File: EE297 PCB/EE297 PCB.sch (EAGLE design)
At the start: 98 parts, among them IC1 MEGA32-P, IC2 MEGA32-P, IC3 7805T, K1 CQ1-12V, K3 CQ1-12V, T1 BC547, T2 TIP122, T3 TIP122, T4 TIP122, T5 BC547

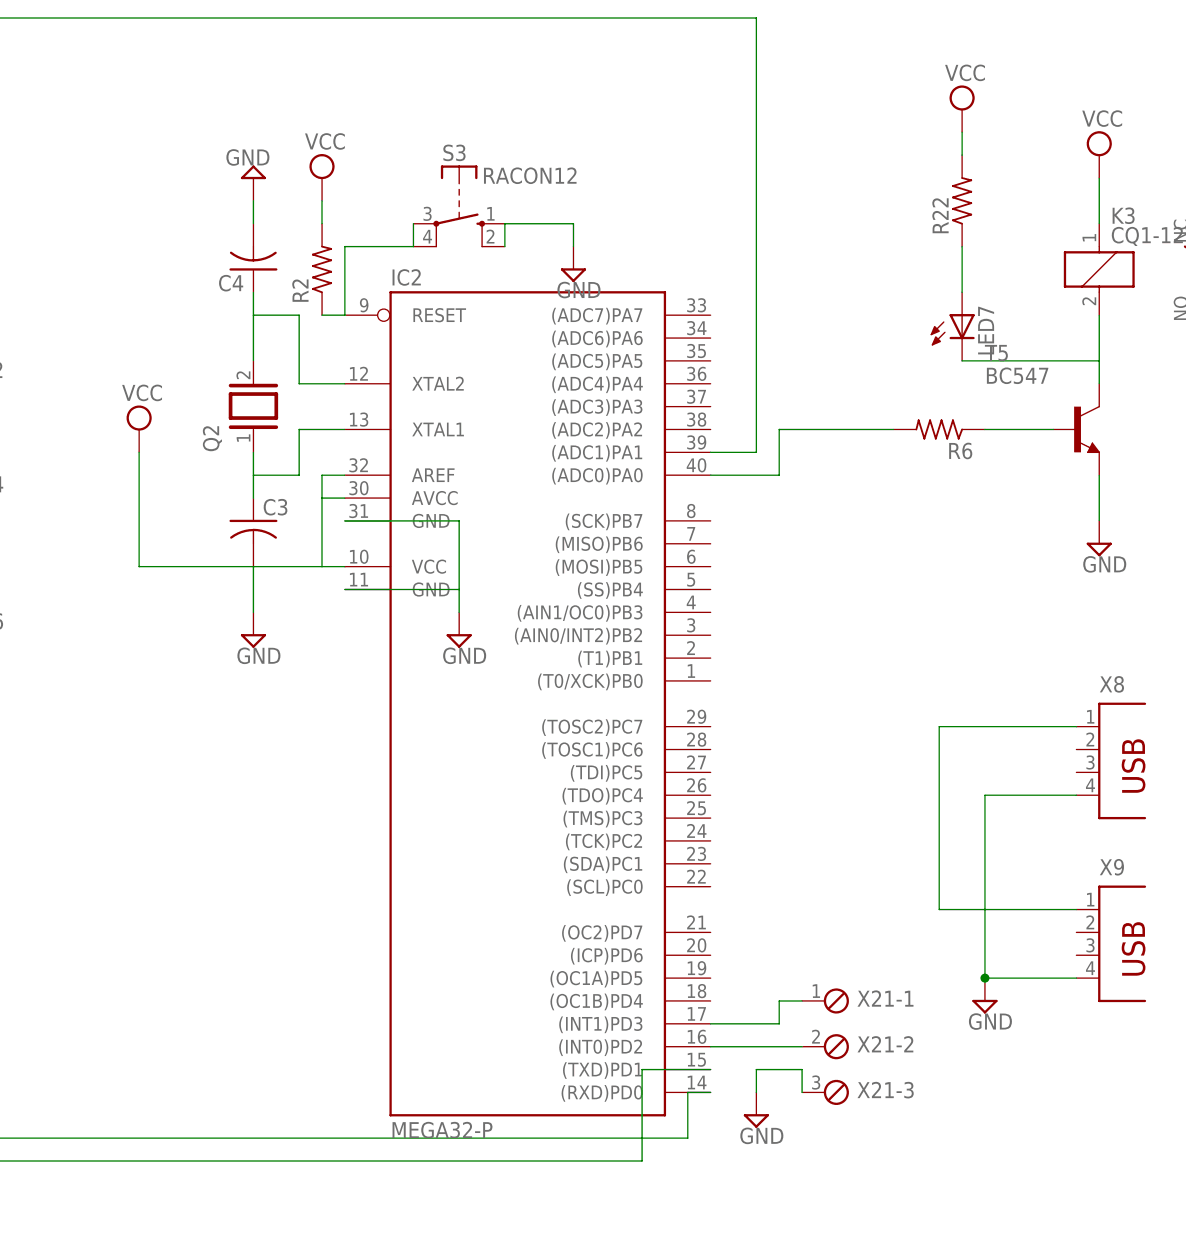
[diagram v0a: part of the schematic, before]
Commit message: MS Project PCB Design Added
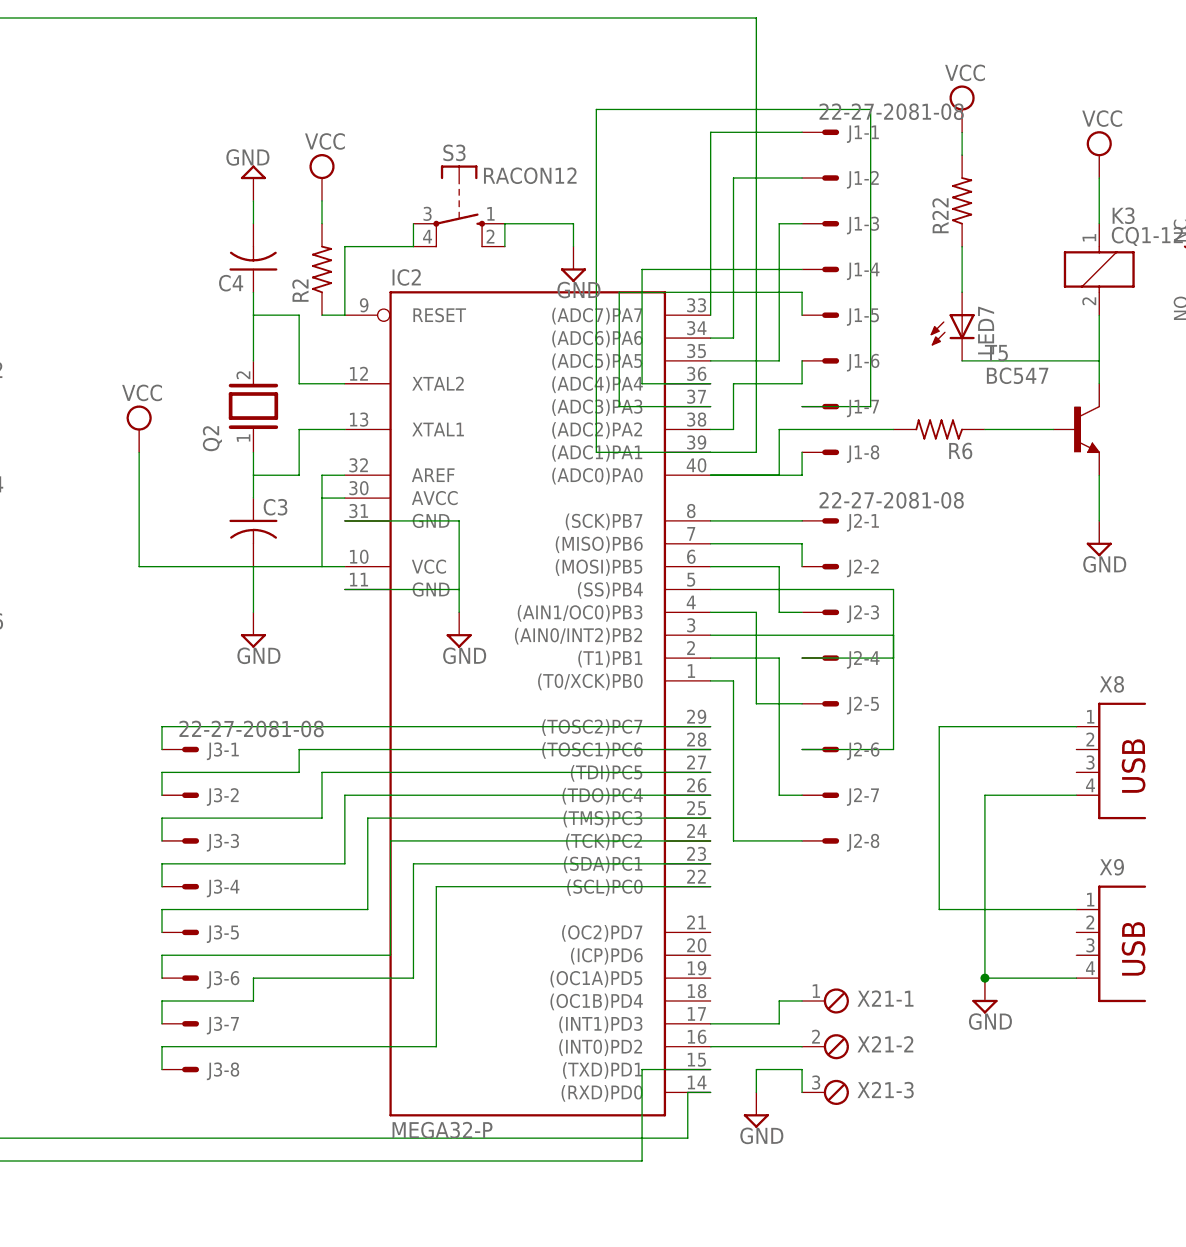
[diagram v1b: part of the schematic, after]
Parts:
- added J1, J2, J3: 22-27-2081-08, con-molex:22-27-2081-08
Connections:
- new net N$157: IC2.(ADC7)PA7, J1-1.S
- new net N$158: IC2.(ADC6)PA6, J1-2.S
- new net N$159: IC2.(ADC5)PA5, J1-3.S
- new net N$160: IC2.(ADC4)PA4, J1-4.S
- new net N$161: IC2.(ADC3)PA3, J1-5.S
- new net N$162: IC2.(ADC2)PA2, J1-6.S
- new net N$164: IC2.(SCK)PB7, J2-1.S
- new net N$165: IC2.(MISO)PB6, J2-2.S
- new net N$166: IC2.(MOSI)PB5, J2-3.S
- new net N$167: IC2.(SS)PB4, J2-4.S
- new net N$168: IC2.(AIN1/OC0)PB3, J2-5.S
- new net N$169: IC2.(AIN0/INT2)PB2, J2-6.S
- new net N$170: IC2.(T1)PB1, J2-7.S
- new net N$171: IC2.(T0/XCK)PB0, J2-8.S
- new net N$172: IC2.(TOSC2)PC7, J3-1.S
- new net N$173: IC2.(TOSC1)PC6, J3-2.S
- new net N$174: IC2.(TDI)PC5, J3-3.S
- new net N$175: IC2.(TDO)PC4, J3-4.S
- new net N$176: IC2.(TMS)PC3, J3-5.S
- new net N$177: IC2.(TCK)PC2, J3-6.S
- new net N$178: IC2.(SDA)PC1, J3-7.S
- new net N$179: IC2.(SCL)PC0, J3-8.S
- net N$44: now also J1-8.S
- net N$45: now also J1-7.S
